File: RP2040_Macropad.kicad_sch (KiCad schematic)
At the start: 0 parts

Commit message: Finished part of the schematic
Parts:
- added C1, C2: 10n, symbol Device:C_Small
- added D1, D10, D2, D3, D4, D5, D6, D7, D8, D9: 1N4148, Diode_THT:D_DO-35_SOD27_P7.62mm_Horizontal, symbol Diode:1N4148
- added D11, D12, D13, D14, D15, D16, D17, D18, D19: SK6812MINI, LED_SMD:LED_SK6812MINI_PLCC4_3.5x3.5mm_P1.75mm, symbol LED:SK6812MINI
- added R1, R2, R3, R4: 10k, symbol Device:R_Small
- added R5: 330, symbol Device:R_Small
- added SW1, SW2, SW3, SW4, SW5, SW6, SW7, SW8, SW9: SW_Push, symbol Switch:SW_Push
- added SW10: RotaryEncoder_Switch, symbol Device:RotaryEncoder_Switch
- added U1: kb2040, symbol kb2040:kb2040
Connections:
- new net: D1.2 (A), SW1.2
- new net: D11.1 (DOUT), D12.3 (DIN)
- new net: D11.3 (DIN), R5.2
- new net: D15.1 (DOUT), D16.3 (DIN)
- new net: D14.1 (DOUT), D15.3 (DIN)
- new net: D18.1 (DOUT), D19.3 (DIN)
- new net: D7.2 (A), SW7.2
- new net: D6.2 (A), SW6.2
- new net: D17.1 (DOUT), D18.3 (DIN)
- new net: D16.1 (DOUT), D17.3 (DIN)
- new net: D13.1 (DOUT), D14.3 (DIN)
- new net: D12.1 (DOUT), D13.3 (DIN)
- new net: R1.2, R3.1, SW10.A
- new net: D2.2 (A), SW2.2
- new net: D4.2 (A), SW4.2
- new net: R2.2, R4.1, SW10.B
- new net: D10.2 (A), SW10.S2
- new net: D5.2 (A), SW5.2
- new net: D3.2 (A), SW3.2
- new net +3.3V: D11.4 (VDD), D12.4 (VDD), D13.4 (VDD), D14.4 (VDD), D15.4 (VDD), D16.4 (VDD), D17.4 (VDD), D18.4 (VDD), D19.4 (VDD), R3.2, R4.2, U1.18 (3.3v)
- new net Col 0: SW1.1, SW10.S1, SW4.1, SW7.1, U1.3 (D1)
- new net Col 1: SW2.1, SW5.1, SW8.1, U1.6 (D2)
- new net Col 2: SW3.1, SW6.1, SW9.1, U1.7 (D3)
- new net Enocder A: C1.2, R1.1, U1.12 (D8)
- new net Enocder B: C2.2, R2.1, U1.13 (D9)
- new net GND: C1.1, C2.1, D11.2 (VSS), D12.2 (VSS), D13.2 (VSS), D14.2 (VSS), D15.2 (VSS), D16.2 (VSS), D17.2 (VSS), D18.2 (VSS), D19.2 (VSS), SW10.C, U1.4 (GND), U1.5 (GND)
- new net LED_Matrix: R5.1, U1.2 (D0)
- new net Row 0: D1.1 (K), D2.1 (K), D3.1 (K), U1.8 (D4)
- new net Row 1: D4.1 (K), D5.1 (K), D6.1 (K), U1.9 (D5)
- new net Row 2: D7.1 (K), D8.1 (K), D9.1 (K), U1.10 (D6)
- new net Row 3: D10.1 (K), U1.11 (D7)

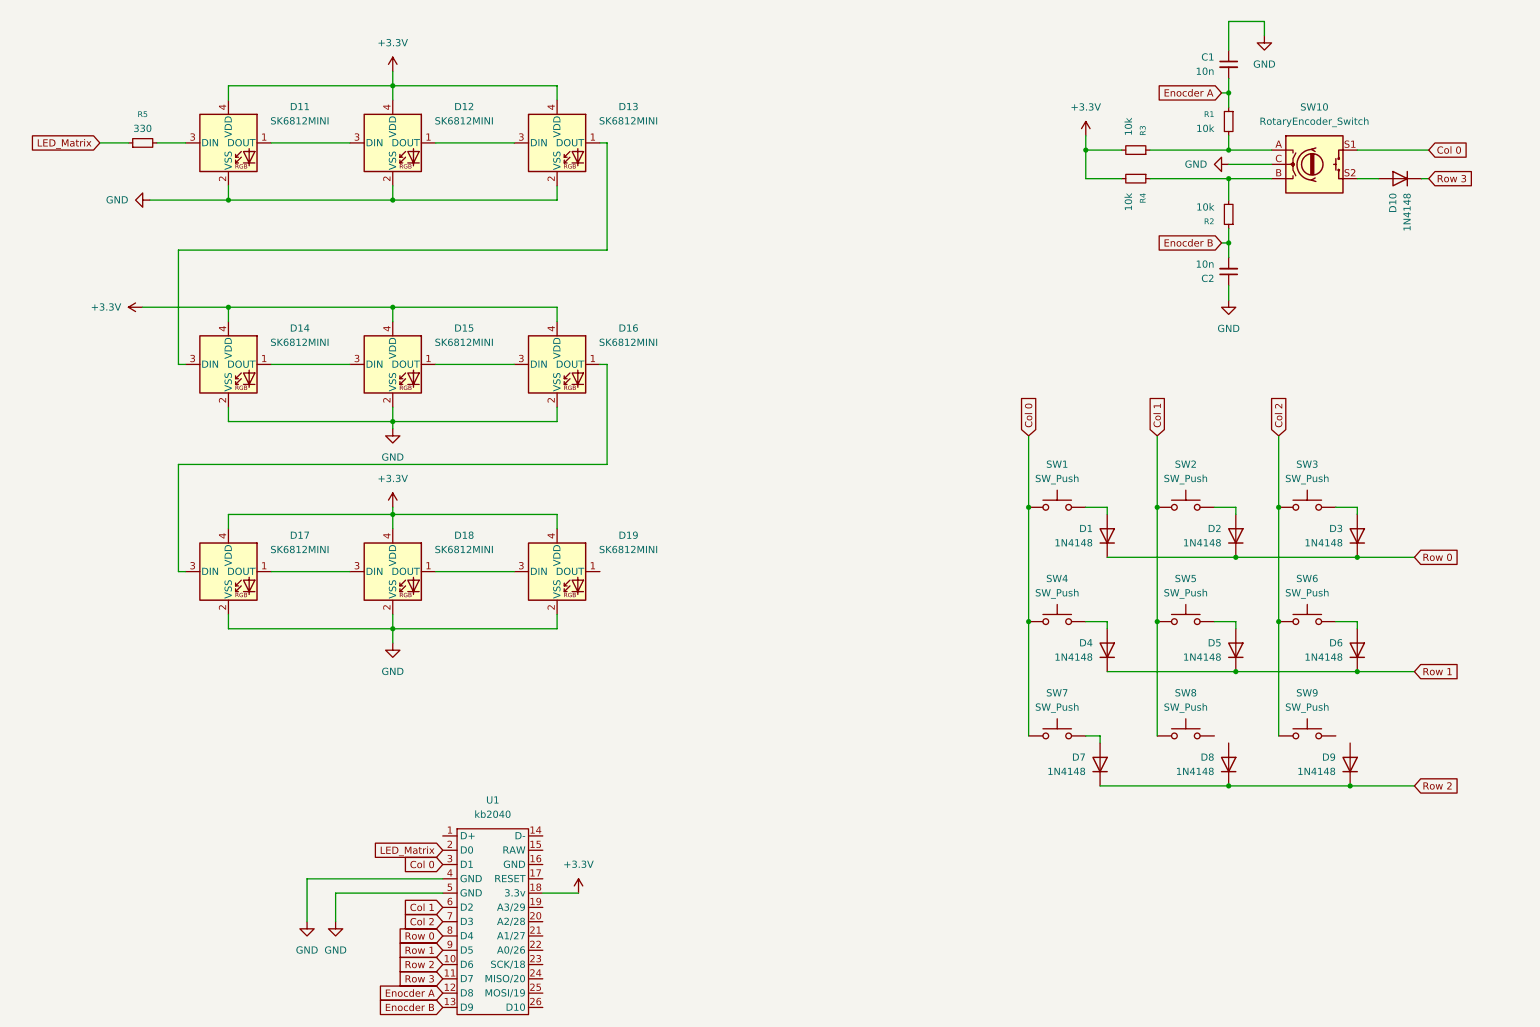
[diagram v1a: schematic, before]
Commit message: Finished schematic, doing layout
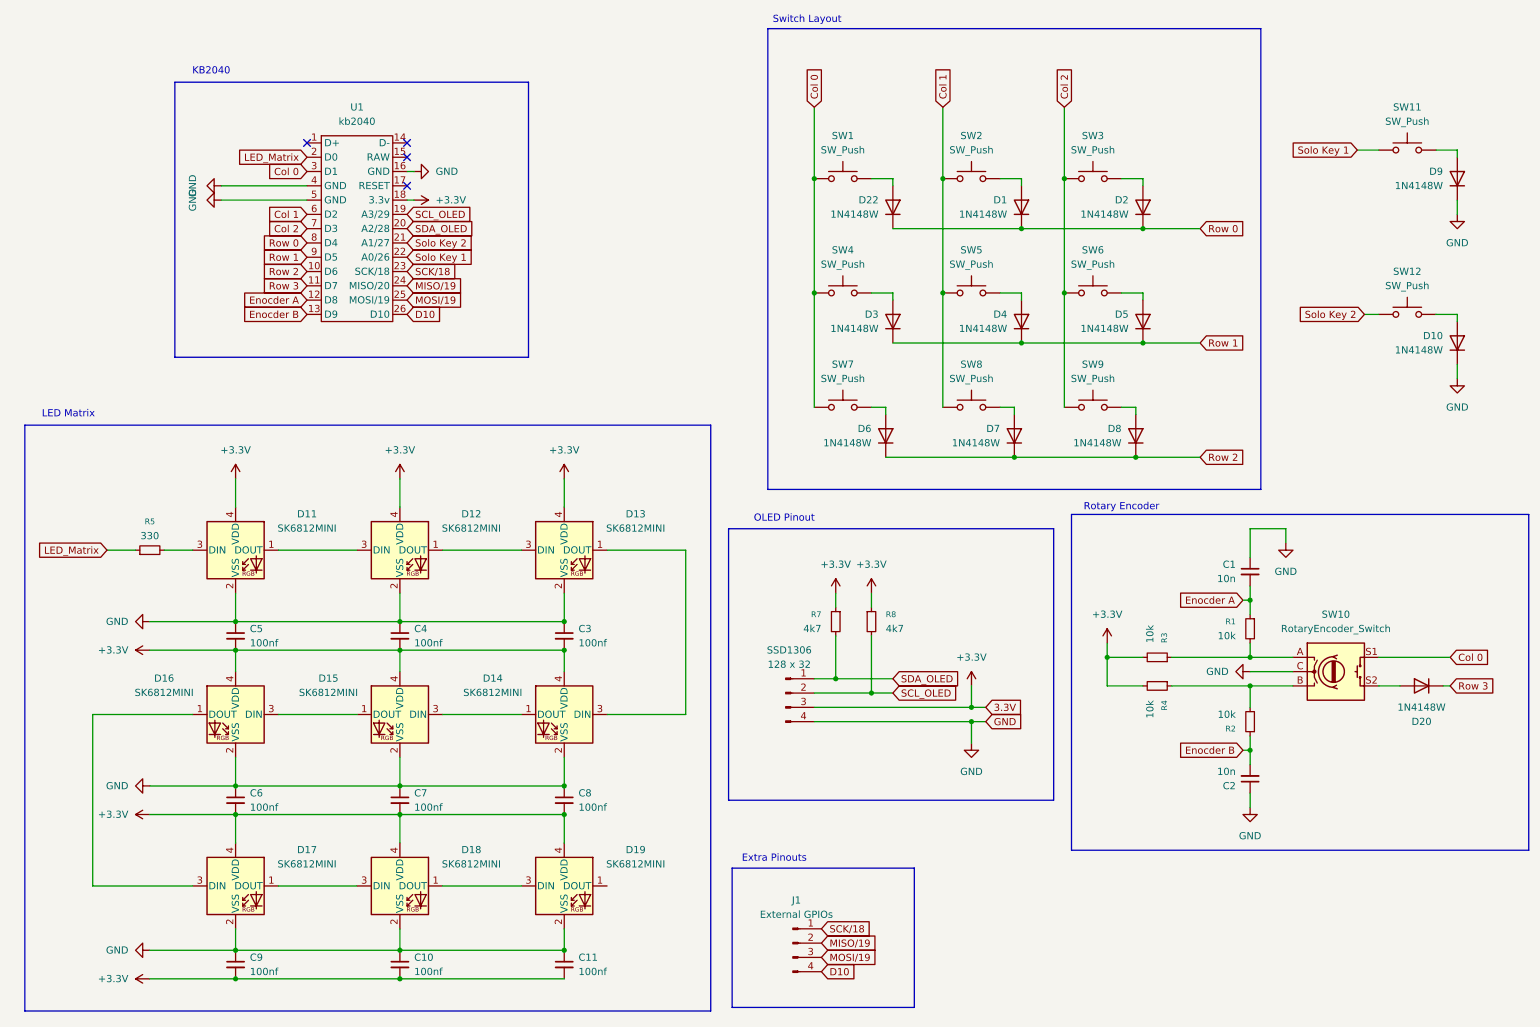
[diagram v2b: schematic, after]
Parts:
- removed D1, D10, D2, D3, D4, D5, D6, D7, D8, D9: 1N4148, Diode_THT:D_DO-35_SOD27_P7.62mm_Horizontal, symbol Diode:1N4148
- added C10, C11, C3, C4, C5, C6, C7, C8, C9: 100nf, Capacitor_SMD:C_0603_1608Metric, symbol Device:C_Small
- added D1, D10, D2, D20, D22, D3, D4, D5, D6, D7, D8, D9: 1N4148W, Diode_SMD:D_SOD-123, symbol Diode:1N4148W
- added J1: External GPIOs, Connector_PinHeader_2.54mm:PinHeader_1x04_P2.54mm_Vertical, symbol Connector:Conn_01x04_Pin
- added R7, R8: 4k7, Resistor_SMD:R_0603_1608Metric, symbol Device:R_Small
- added SSD1306: 128 x 32, Connector_PinHeader_2.54mm:PinHeader_1x04_P2.54mm_Vertical, symbol Connector:Conn_01x04_Pin
- added SW11, SW12: SW_Push, PCM_Switch_Keyboard_Hotswap_Kailh:SW_Hotswap_Kailh_MX_1.00u, symbol Switch:SW_Push
- C1, C2: footprint (none) -> Capacitor_SMD:C_0603_1608Metric
- R1, R2, R3, R4, R5: footprint (none) -> Resistor_SMD:R_0603_1608Metric
- SW1, SW2, SW3, SW4, SW5, SW6, SW7, SW8, SW9: footprint (none) -> PCM_Switch_Keyboard_Hotswap_Kailh:SW_Hotswap_Kailh_MX_1.00u
- SW10: footprint (none) -> Rotary_Encoder:RotaryEncoder_Alps_EC11E-Switch_Vertical_H20mm
- U1: footprint (none) -> footprints:kb2040
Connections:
- net +3.3V: now also C10.2, C11.2, C3.2, C4.2, C5.2, C6.2, C7.2, C8.2, C9.2, R7.1, R8.1, SSD1306.3 (Pin_3)
- net GND: now also U1.16 (GND), C10.1, C11.1, C3.1, C4.1, C5.1, C6.1, C7.1, C8.1, C9.1, D10.1 (K), D9.1 (K), SSD1306.4 (Pin_4)
- net Row 0: now also D1.1 (K), D2.1 (K), D22.1 (K)
- net Row 1: now also D3.1 (K), D4.1 (K), D5.1 (K)
- net Row 2: now also D6.1 (K), D7.1 (K), D8.1 (K)
- net Row 3: now also D20.1 (K)
- net at SW1.2: now also D22.2 (A)
- net SCL_OLED: now reaches U1.19 (A3/29)
- net SCL_OLED: now also R8.2, SSD1306.2 (Pin_2)
- net SDA_OLED: now reaches U1.20 (A2/28)
- net SDA_OLED: now also R7.2, SSD1306.1 (Pin_1)
- net Solo Key 2: now reaches U1.21 (A1/27)
- net Solo Key 2: now also SW12.1
- net Solo Key 1: now reaches U1.22 (A0/26)
- net Solo Key 1: now also SW11.1
- net SCK/18: now reaches U1.23 (SCK/18)
- net SCK/18: now also J1.1 (Pin_1)
- net MISO/19: now reaches U1.24 (MISO/20)
- net MISO/19: now also J1.2 (Pin_2)
- net MOSI/19: now reaches U1.25 (MOSI/19)
- net MOSI/19: now also J1.3 (Pin_3)
- net D10: now reaches U1.26 (D10)
- net D10: now also J1.4 (Pin_4)
- net at SW7.2: now also D6.2 (A)
- net at SW8.2: now also D7.2 (A)
- net at SW6.2: now also D5.2 (A)
- net at SW9.2: now also D8.2 (A)
- net at SW2.2: now also D1.2 (A)
- net at SW4.2: now also D3.2 (A)
- net at SW10.S2: now also D20.2 (A)
- net at SW5.2: now also D4.2 (A)
- net at SW3.2: now also D2.2 (A)
- new net: D9.2 (A), SW11.2
- new net: D10.2 (A), SW12.2
- no-connect marks 0 -> 4
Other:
- note added: "Extra Pinouts"
- note added: "KB2040"
- note added: "LED Matrix"
- note added: "OLED Pinout"
- note added: "Rotary Encoder"
- note added: "Switch Layout"
- moved on the sheet: C1, C2, D11, D12, D13, D14, D15, D16, D17, D18, D19, R1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

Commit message: layout complete
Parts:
- removed C1, C2: 10n, Capacitor_SMD:C_0603_1608Metric, symbol Device:C_Small
- removed D11, D12, D13, D14, D15, D16, D17, D18, D19: SK6812MINI, LED_SMD:LED_SK6812MINI_PLCC4_3.5x3.5mm_P1.75mm, symbol LED:SK6812MINI
- removed D20, D22: 1N4148W, Diode_SMD:D_SOD-123, symbol Diode:1N4148W
- removed J1: External GPIOs, Connector_PinHeader_2.54mm:PinHeader_1x04_P2.54mm_Vertical, symbol Connector:Conn_01x04_Pin
- removed R1, R2, R3, R4: 10k, Resistor_SMD:R_0603_1608Metric, symbol Device:R_Small
- added C10, C11: 100nf, Capacitor_SMD:C_0603_1608Metric, symbol Device:C_Small
- added D3, D4: 1N4148W, Diode_SMD:D_SOD-123, symbol Diode:1N4148W
- added H1, H2, H3, H4: MountingHole_Pad, MountingHole:MountingHole_3.2mm_M3_DIN965_Pad, symbol Mechanical:MountingHole_Pad
- added LED1, LED10, LED11, LED2, LED3, LED4, LED5, LED6, LED7, LED8, LED9: MX_SK6812MINI-E, PCM_marbastlib-mx:LED_MX_6028R, symbol PCM_marbastlib-mx:MX_SK6812MINI-E
- renumbered C5 to C1, C4 to C2, C8 to C4, C7 to C5, C11 to C7, C10 to C8, D10 to D1, D6 to D10, D7 to D11, D8 to D12, D9 to D2, D1 to D5, D2 to D6, D3 to D7, D4 to D8, D5 to D9, SW12 to SW1, SW7 to SW10, SW8 to SW11, SW9 to SW12, SW11 to SW2, SW10 to SW3, SW1 to SW4, SW2 to SW5, SW3 to SW6, SW4 to SW7, SW5 to SW8, SW6 to SW9
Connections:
- net +3.3V: now also C10.2, C11.2, LED1.1 (VDD), LED10.1 (VDD), LED11.1 (VDD), LED2.1 (VDD), LED3.1 (VDD), LED4.1 (VDD), LED5.1 (VDD), LED6.1 (VDD), LED7.1 (VDD), LED8.1 (VDD), LED9.1 (VDD)
- net Col 1: now also SW1.1, SW10.1, SW4.1, SW7.1, U1.3 (D1); no longer SW11.1, SW5.1, SW8.1, U1.6 (D2)
- net Col 2: now also SW11.1, SW2.1, SW5.1, SW8.1, U1.6 (D2); no longer SW12.1, SW6.1, SW9.1, U1.7 (D3)
- net Enocder A: now also SW3.A; no longer U1.12 (D8)
- net Enocder B: now also SW3.B; no longer U1.13 (D9)
- net GND: now also C10.1, C11.1, H1.1, H2.1, H3.1, H4.1, LED1.4 (VSS), LED10.4 (VSS), LED11.4 (VSS), LED2.4 (VSS), LED3.4 (VSS), LED4.4 (VSS), LED5.4 (VSS), LED6.4 (VSS), LED7.4 (VSS), LED8.4 (VSS), LED9.4 (VSS); no longer D1.1 (K), D2.1 (K)
- net Row 1: now also D1.1 (K), D2.1 (K), U1.8 (D4), D3.1 (K); no longer D7.1 (K), D8.1 (K), D9.1 (K), U1.9 (D5)
- net Row 2: now also D5.1 (K), D6.1 (K), U1.9 (D5), D4.1 (K); no longer D10.1 (K), D11.1 (K), D12.1 (K), U1.10 (D6)
- net Row 3: now also D7.1 (K), D8.1 (K), D9.1 (K), U1.10 (D6); no longer U1.11 (D7)
- net at SW4.2: now also D4.2 (A)
- net at R5.2: now also LED1.3 (DIN)
- net at SW3.S2: now also D3.2 (A)
- removed net Col 0: SW10.1, SW3.S1, SW4.1, SW7.1, U1.3 (D1)
- removed net Row 0: D5.1 (K), D6.1 (K), U1.8 (D4)
- net Solo Key 1 renamed A0
- net A0: no longer SW2.1
- net Solo Key 2 renamed A1
- net A1: no longer SW1.1
- new net: LED1.2 (DOUT), LED2.3 (DIN)
- new net: LED4.2 (DOUT), LED5.3 (DIN)
- new net: LED3.2 (DOUT), LED4.3 (DIN)
- new net: LED10.3 (DIN), LED7.2 (DOUT)
- new net: LED7.3 (DIN), LED8.2 (DOUT)
- new net: LED2.2 (DOUT), LED3.3 (DIN)
- new net: LED10.2 (DOUT), LED11.3 (DIN)
- new net: LED8.3 (DIN), LED9.2 (DOUT)
- new net: LED6.2 (DOUT), LED9.3 (DIN)
- new net: LED5.2 (DOUT), LED6.3 (DIN)
- new net Col 3: SW12.1, SW3.S1, SW6.1, SW9.1, U1.7 (D3)
- new net D8: U1.12 (D8)
- new net D9: U1.13 (D9)
- new net Row 4: D10.1 (K), D11.1 (K), D12.1 (K), U1.11 (D7)
- no-connect marks 4 -> 5
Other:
- note added: "Switch Matrix"
- note removed: "Extra Pinouts"
- note removed: "Rotary Encoder"
- note removed: "Switch Layout"
- moved on the sheet: C1, C2, C3, C4, C5, C6, C7, C8, C9, D1, D10, D11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
